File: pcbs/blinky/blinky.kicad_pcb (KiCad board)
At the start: 4 copper layers, 135 x 97 mm, 178 parts, among them J1 JACK IN, J3 CA1-9, J4 CB1-9, Q1 PMBT2222A,215, SW1 TACTILE, SW2 JS202011JCQN, U1 ATSAMD21E17, U2 MIC5225-3.3YM5, U3 TSOP36438TT, U4 IS31FL3731-SALS2

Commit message: Put all the passive values on silkscreen
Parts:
- C1: value 100uF 6.3V -> 100u
- C10, C11: value 10uF -> 10u
- C2, C7: value 1uF -> 1u
- C3, C4, C8, C9: value 0.1uF -> 0.1
- C5: value 1.0uF -> 1u
- C6: value 2.2uF -> 2.2
- R1: value 10kΩ -> 10k
- R2: value 330Ω -> 330
- R3: value 47Ω -> 47
- R4: value 470Ω -> 470
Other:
- board text added: "+"
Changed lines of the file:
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@@
   (general
     (thickness 1.6)
-    (drawings 20)
+    (drawings 21)
     (tracks 946)
     (zones 0)
@@
     (tags resistor)
     (attr smd)
-    (fp_text reference R10 (at -3.2 0 90) (layer F.SilkS)
+    (fp_text reference R10 (at -3.2 0 90) (layer F.Fab)
       (effects (font (size 1 1) (thickness 0.15)))
     )
-    (fp_text value 20K (at 0 1.43 90) (layer F.Fab)
+    (fp_text value 20K (at -2.969 0.023 90) (layer F.SilkS)
       (effects (font (size 1 1) (thickness 0.15)))
     )
@@
     (tags resistor)
     (attr smd)
-    (fp_text reference R9 (at 2.8 0 90) (layer F.SilkS)
+    (fp_text reference R9 (at 2.8 0 90) (layer F.Fab)
       (effects (font (size 1 1) (thickness 0.15)))
     )
-    (fp_text value 20K (at 0 1.43 90) (layer F.Fab)
+    (fp_text value 20K (at 2.969 -0.045 90) (layer F.SilkS)
       (effects (font (size 1 1) (thickness 0.15)))
     )
@@
     (tags resistor)
     (attr smd)
-    (fp_text reference R8 (at 2.8 0 90) (layer F.SilkS)
+    (fp_text reference R8 (at 2.8 0 90) (layer F.Fab)
       (effects (font (size 1 1) (thickness 0.15)))
     )
-    (fp_text value 20K (at 0 1.43 90) (layer F.Fab)
+    (fp_text value 20K (at 2.969 -0.194 90) (layer F.SilkS)
       (effects (font (size 1 1) (thickness 0.15)))
     )
@@
     (tags resistor)
     (attr smd)
-    (fp_text reference R7 (at -2.6 0 90) (layer F.SilkS)
+    (fp_text reference R7 (at -2.6 0 90) (layer F.Fab)
       (effects (font (size 1 1) (thickness 0.15)))
     )
-    (fp_text value 20K (at 0 1.43 90) (layer F.Fab)
+    (fp_text value 20K (at -3.111 0.067 90) (layer F.SilkS)
       (effects (font (size 1 1) (thickness 0.15)))
     )
@@
     (tags resistor)
     (attr smd)
-    (fp_text reference R6 (at 0 -1.43) (layer F.SilkS)
+    (fp_text reference R6 (at 0 -1.43) (layer F.Fab)
       (effects (font (size 1 1) (thickness 0.15)))
     )
-    (fp_text value 20K (at 0 1.43) (layer F.Fab)
+    (fp_text value 20K (at 0 -1.418) (layer F.SilkS)
       (effects (font (size 1 1) (thickness 0.15)))
     )
@@
     (tags resistor)
     (attr smd)
-    (fp_text reference R5 (at 0 -1.43) (layer F.SilkS)
+    (fp_text reference R5 (at 0 -1.43) (layer F.Fab)
       (effects (font (size 1 1) (thickness 0.15)))
     )
-    (fp_text value 20K (at 0 1.43) (layer F.Fab)
+    (fp_text value 20K (at 0.089 -1.481) (layer F.SilkS)
       (effects (font (size 1 1) (thickness 0.15)))
     )
@@
     (tags resistor)
     (attr smd)
-    (fp_text reference R4 (at -2.6 0 90) (layer F.SilkS)
+    (fp_text reference R4 (at -2.6 0 90) (layer F.Fab)
       (effects (font (size 1 1) (thickness 0.15)))
     )
-    (fp_text value 470Ω (at 0 1.43 90) (layer F.Fab)
+    (fp_text value 470 (at 2.96 0.15 90) (layer F.SilkS)
       (effects (font (size 1 1) (thickness 0.15)))
     )
@@
     (tags resistor)
     (attr smd)
-    (fp_text reference R3 (at 2.6 0 90) (layer F.SilkS)
+    (fp_text reference R3 (at 2.6 0 90) (layer F.Fab)
       (effects (font (size 1 1) (thickness 0.15)))
     )
-    (fp_text value 47Ω (at 0 1.43 90) (layer F.Fab)
+    (fp_text value 47 (at -2.706 -0.105 90) (layer F.SilkS)
       (effects (font (size 1 1) (thickness 0.15)))
     )
@@
     (tags resistor)
     (attr smd)
-    (fp_text reference R2 (at -2.8 0.2) (layer F.SilkS)
+    (fp_text reference R2 (at -2.8 0.2) (layer F.Fab)
       (effects (font (size 1 1) (thickness 0.15)))
     )
-    (fp_text value 330Ω (at 0 1.43) (layer F.Fab)
+    (fp_text value 330 (at -3.111 -0.097) (layer F.SilkS)
       (effects (font (size 1 1) (thickness 0.15)))
     )
@@
     (tags resistor)
     (attr smd)
-    (fp_text reference R1 (at -2.8 0) (layer F.SilkS)
+    (fp_text reference R1 (at -2.8 0) (layer F.Fab)
       (effects (font (size 1 1) (thickness 0.15)))
     )
-    (fp_text value 10kΩ (at 0 1.43) (layer F.Fab)
+    (fp_text value 10k (at -2.984 -0.192) (layer F.SilkS)
       (effects (font (size 1 1) (thickness 0.15)))
     )
@@
     (tags capacitor)
     (attr smd)
-    (fp_text reference C11 (at 3 0.2 90) (layer F.SilkS)
+    (fp_text reference C11 (at 3 0.2 90) (layer F.Fab)
       (effects (font (size 1 1) (thickness 0.15)))
     )
-    (fp_text value 10uF (at 0 1.43 90) (layer F.Fab)
+    (fp_text value 10u (at 2.984 -0.001 90) (layer F.SilkS)
       (effects (font (size 1 1) (thickness 0.15)))
     )
@@
     (tags capacitor)
     (attr smd)
-    (fp_text reference C10 (at 3 0 90) (layer F.SilkS)
+    (fp_text reference C10 (at 3 0 90) (layer F.Fab)
       (effects (font (size 1 1) (thickness 0.15)))
     )
-    (fp_text value 10uF (at 0 1.43 90) (layer F.Fab)
+    (fp_text value 10u (at 2.984 -0.023 90) (layer F.SilkS)
       (effects (font (size 1 1) (thickness 0.15)))
     )
@@
     (tags capacitor)
     (attr smd)
-    (fp_text reference C9 (at 2.6 0 90) (layer F.SilkS)
+    (fp_text reference C9 (at 2.6 0 90) (layer F.Fab)
       (effects (font (size 1 1) (thickness 0.15)))
     )
-    (fp_text value 0.1uF (at 0 1.43 90) (layer F.Fab)
+    (fp_text value 0.1 (at 2.857 -0.045 90) (layer F.SilkS)
       (effects (font (size 1 1) (thickness 0.15)))
     )
@@
     (tags capacitor)
     (attr smd)
-    (fp_text reference C8 (at -2.8 0 90) (layer F.SilkS)
+    (fp_text reference C8 (at -2.8 0 90) (layer F.Fab)
       (effects (font (size 1 1) (thickness 0.15)))
     )
-    (fp_text value 0.1uF (at 0 1.43 90) (layer F.Fab)
+    (fp_text value 0.1 (at -2.588 0.001 90) (layer F.SilkS)
       (effects (font (size 1 1) (thickness 0.15)))
     )
@@
     (tags capacitor)
     (attr smd)
-    (fp_text reference C7 (at -2.6 0.2 90) (layer F.SilkS)
+    (fp_text reference C7 (at -2.6 0.2 90) (layer F.Fab)
       (effects (font (size 1 1) (thickness 0.15)))
     )
-    (fp_text value 1uF (at 0 1.43 90) (layer F.Fab)
+    (fp_text value 1u (at 2.96 -0.063 90) (layer F.SilkS)
       (effects (font (size 1 1) (thickness 0.15)))
     )
@@
     (tags capacitor)
     (attr smd)
-    (fp_text reference C6 (at -3 0 90) (layer F.SilkS)
+    (fp_text reference C6 (at -3 0 90) (layer F.Fab)
       (effects (font (size 1 1) (thickness 0.15)))
     )
-    (fp_text value 2.2uF (at 0 1.43 90) (layer F.Fab)
+    (fp_text value 2.2 (at -3.302 -0.127 180) (layer F.SilkS)
       (effects (font (size 1 1) (thickness 0.15)))
     )
@@
     (tags capacitor)
     (attr smd)
-    (fp_text reference C5 (at -3.048 0.127 90) (layer F.SilkS)
+    (fp_text reference C5 (at -3.048 0.127 90) (layer F.Fab)
       (effects (font (size 1 1) (thickness 0.15)))
     )
-    (fp_text value 1.0uF (at 0 1.43 90) (layer F.Fab)
+    (fp_text value 1u (at -3.302 0 180) (layer F.SilkS)
       (effects (font (size 1 1) (thickness 0.15)))
     )
@@
     (tags capacitor)
     (attr smd)
-    (fp_text reference C4 (at 2.8 0) (layer F.SilkS)
+    (fp_text reference C4 (at 2.8 0) (layer F.Fab)
       (effects (font (size 1 1) (thickness 0.15)))
     )
-    (fp_text value 0.1uF (at 0 1.43) (layer F.Fab)
+    (fp_text value 0.1 (at 2.857 -0.094) (layer F.SilkS)
       (effects (font (size 1 1) (thickness 0.15)))
     )
@@
     (tags capacitor)
     (attr smd)
-    (fp_text reference C3 (at 2.413 0 180) (layer F.SilkS)
+    (fp_text reference C3 (at 2.413 0 180) (layer F.Fab)
       (effects (font (size 1 1) (thickness 0.15)))
     )
-    (fp_text value 0.1uF (at 0 1.43 90) (layer F.Fab)
+    (fp_text value 0.1 (at 2.159 0 180) (layer F.SilkS)
       (effects (font (size 1 1) (thickness 0.15)))
     )
@@
     (tags capacitor)
     (attr smd)
-    (fp_text reference C2 (at 2.413 0.127 180) (layer F.SilkS)
+    (fp_text reference C2 (at 2.413 0.127 180) (layer F.Fab)
       (effects (font (size 1 1) (thickness 0.15)))
     )
-    (fp_text value 1uF (at 0 1.43 90) (layer F.Fab)
+    (fp_text value 1u (at 2.413 0 180) (layer F.SilkS)
       (effects (font (size 1 1) (thickness 0.15)))
     )
@@
     (tags capacitor)
     (attr smd)
-    (fp_text reference C1 (at -3.937 0.127 270) (layer F.SilkS)
+    (fp_text reference C1 (at -3.937 0.127 270) (layer F.Fab)
       (effects (font (size 1 1) (thickness 0.15)))
     )
-    (fp_text value "100uF 6.3V" (at 0 1.85 90) (layer F.Fab)
+    (fp_text value 100u (at -4.953 0.127 90) (layer F.SilkS)
       (effects (font (size 1 1) (thickness 0.15)))
     )
@@
     )
   )
+  (gr_text + (at 99.993 141.575) (layer F.SilkS)
+    (effects (font (size 1 1) (thickness 0.15)))
+  )
   (gr_text OFF (at 56.94 140.559) (layer F.SilkS)
     (effects (font (size 1 1) (thickness 0.15)))
@@
   (segment (start 76.278 98.304) (end 94.272 98.304) (width 0.2) (layer In1.Cu) (net 14))
   (segment (start 71.926 102.656) (end 76.278 98.304) (width 0.2) (layer In1.Cu) (net 14))
-  (segment (start 99.247 115.304) (end 99.272 115.279) (width 0.2) (layer F.Cu) (net 14))
-  (segment (start 95.072 115.304) (end 99.247 115.304) (width 0.2) (layer F.Cu) (net 14))
-  (segment (start 95.072 115.304) (end 94.672 113.704) (width 0.2) (layer In1.Cu) (net 14))
-  (segment (start 94.472 98.504) (end 94.272 98.304) (width 0.2) (layer In1.Cu) (net 14))
   (segment (start 94.672 98.704) (end 94.472 98.504) (width 0.2) (layer In1.Cu) (net 14))
   (segment (start 94.672 113.704) (end 94.672 98.704) (width 0.2) (layer In1.Cu) (net 14))
-  (via (at 95.072 115.304) (size 0.6) (drill 0.3) (layers F.Cu B.Cu) (net 14))
+  (segment (start 94.472 98.504) (end 94.272 98.304) (width 0.2) (layer In1.Cu) (net 14))
+  (via (at 94.659 115.286) (size 0.6) (drill 0.3) (layers F.Cu B.Cu) (net 14))
+  (segment (start 94.659 115.286) (end 94.672 113.704) (width 0.2) (layer In1.Cu) (net 14))
+  (segment (start 99.247 115.304) (end 99.272 115.279) (width 0.2) (layer F.Cu) (net 14))
+  (segment (start 94.659 115.286) (end 99.247 115.304) (width 0.2) (layer F.Cu) (net 14))
   (via (at 72.823 108.684) (size 0.6) (drill 0.3) (layers F.Cu B.Cu) (net 15))
   (via (at 72.823 111.354) (size 0.6) (drill 0.3) (layers F.Cu B.Cu) (net 15))

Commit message: route sda/scl across the middle
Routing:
- net /SCL: track 124.1 -> 75.7 mm
- net /SDA: track 120.1 -> 73.1 mm, vias 0 -> 2
- net /CB1: track 102.2 -> 104.7 mm, vias 8 -> 7

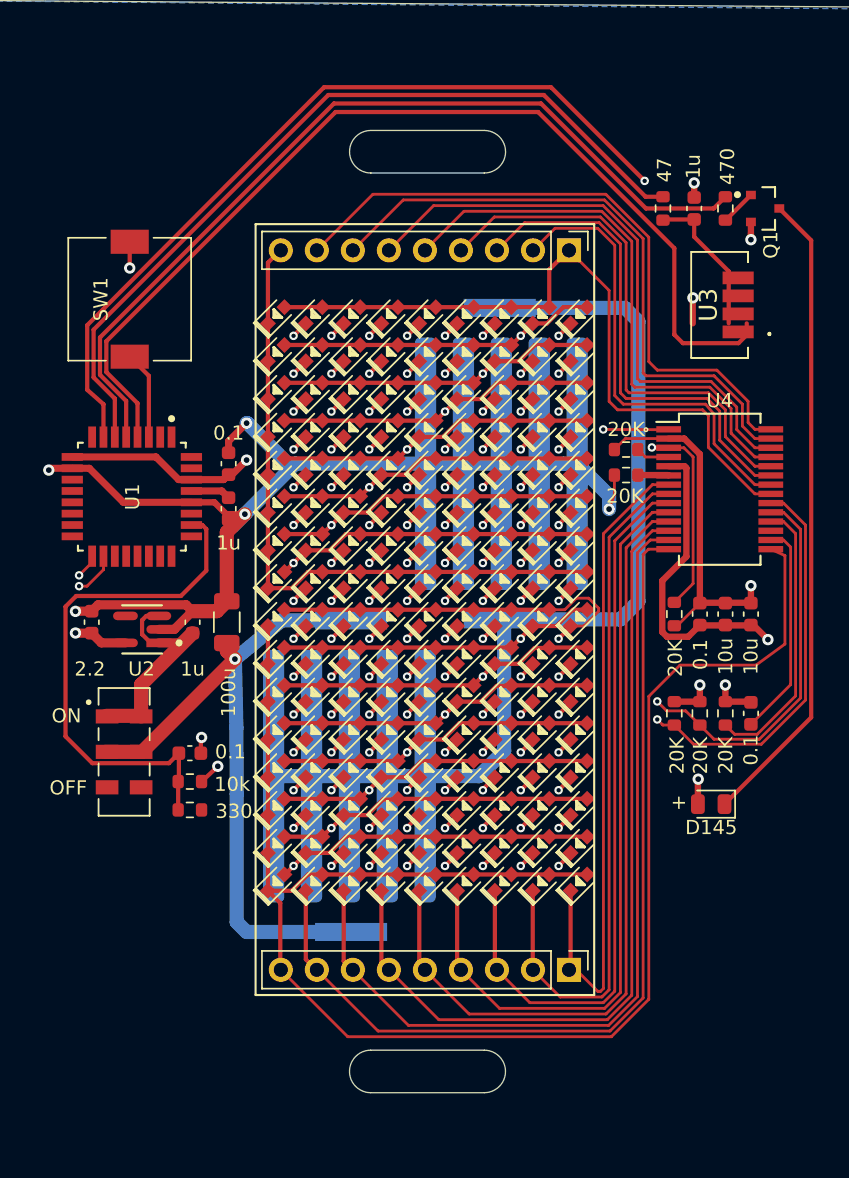
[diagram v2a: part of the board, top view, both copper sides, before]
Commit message: tidied up a bit more routing to make board smaller
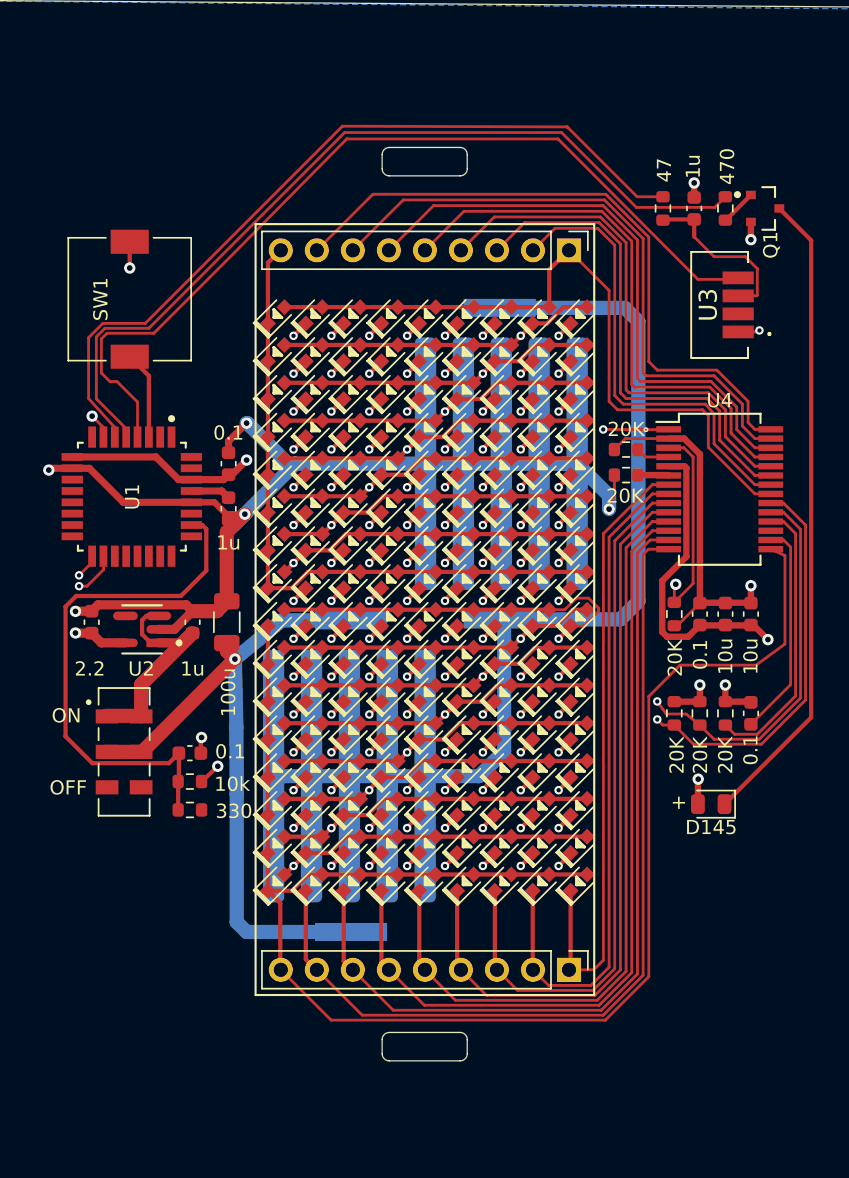
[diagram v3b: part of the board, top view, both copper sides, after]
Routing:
- net /A6: track 90.5 -> 68.1 mm
- net /A1: track 70.9 -> 62.1 mm
- net /CB1: track 104.7 -> 102.8 mm
- net /CB9: track 116.3 -> 114.4 mm
- net /CB8: track 119.0 -> 117.1 mm
- net /CB7: track 116.2 -> 114.4 mm
- net /CB6: track 113.5 -> 111.7 mm
- net /CB5: track 110.9 -> 109.2 mm
- net /A3: track 58.2 -> 56.4 mm
- net /CB4: track 108.3 -> 106.6 mm
- net /CB3: track 105.7 -> 104.0 mm
- net /CB2: track 103.0 -> 101.4 mm
- net Net-(C7-Pad1): track 10.6 -> 12.1 mm
- net /A2: track 62.1 -> 60.8 mm
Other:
- outline, holes or cut-outs redrawn

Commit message: lots of beautiful decorations
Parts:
- moved Q1 42.3 mm to (100.7, 141.7)
- moved J1 23.7 mm to (65.7, 155.3), turned to 323 degrees
- moved D145 3.81 mm to (106.1, 141.5), turned to 0 degrees
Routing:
- net (no net): track 0.00 -> 270.2 mm
- net Net-(Q1-Pad1): track 2.54 -> 49.2 mm
- net /A7: track 0.00 -> 46.1 mm
- net Net-(D145-Pad1): track 45.5 -> 3.55 mm
- net /SWDIO: track 0.00 -> 41.5 mm, vias 0 -> 1
- net /SWCLK: track 0.00 -> 39.1 mm, vias 0 -> 1
- net /~RESET: track 0.00 -> 15.2 mm, vias 0 -> 1
- net VBUS: track 49.2 -> 55.0 mm, vias 1 -> 2
- net +3V3: track 48.2 -> 50.3 mm, vias 6 -> 7
- net GND: track 110.7 -> 111.7 mm, vias 12 -> 13
- added copper zone on F.Cu, net (none)
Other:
- board size 135 x 97 mm -> 91 x 93 mm

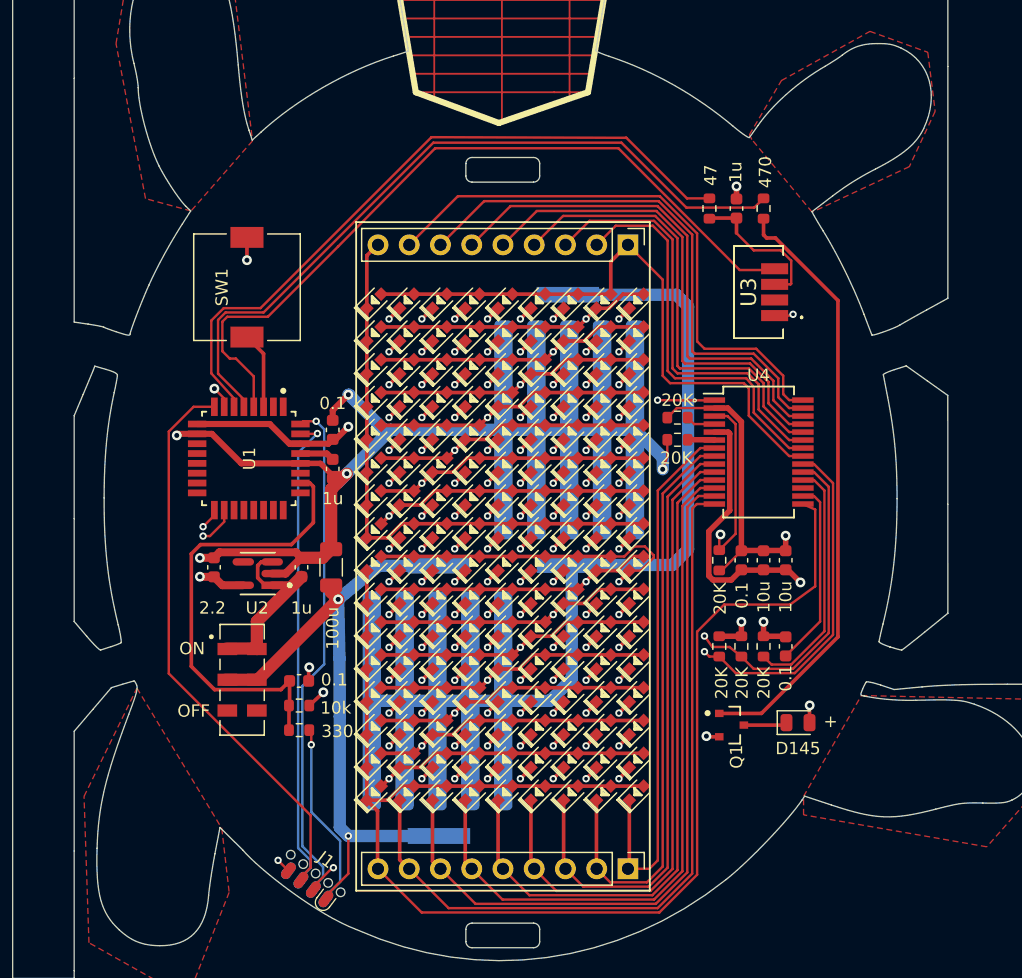
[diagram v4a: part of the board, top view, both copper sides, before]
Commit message: mousebite improvements
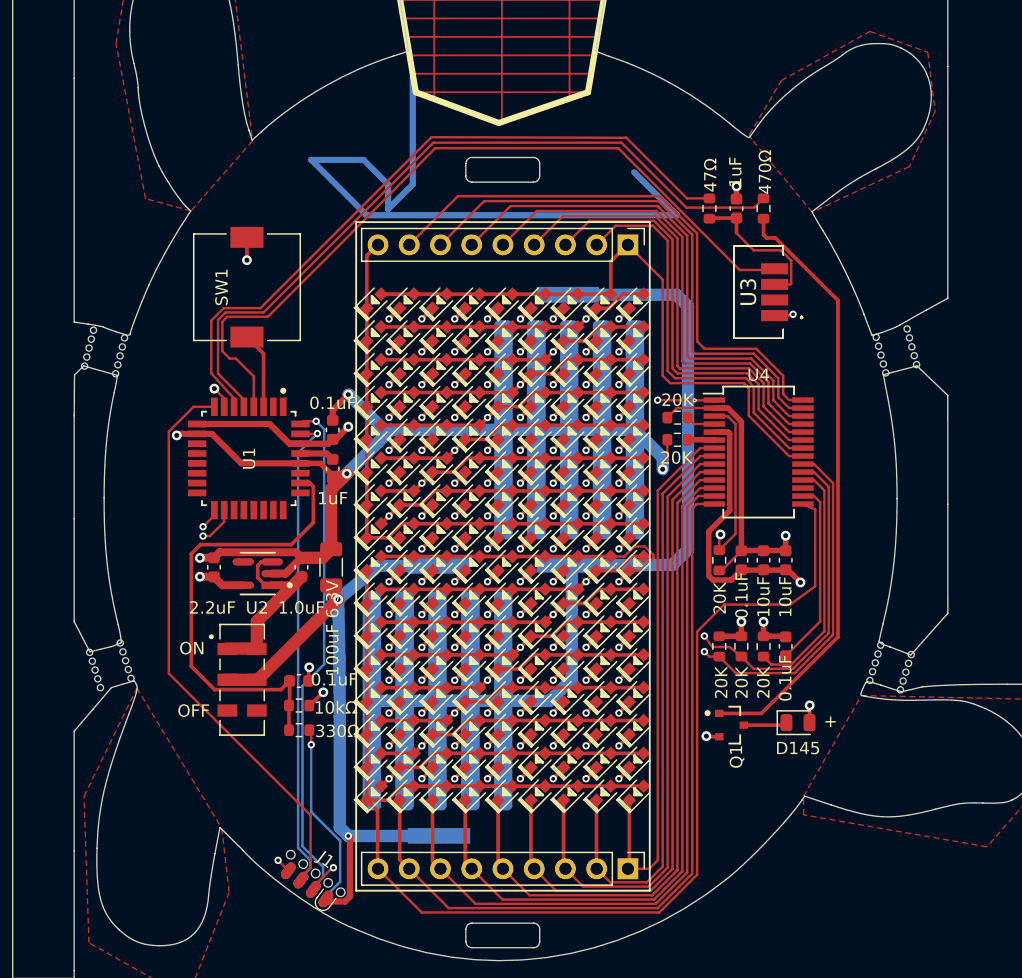
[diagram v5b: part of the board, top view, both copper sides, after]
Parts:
- added H1: Mouse Bite, Joels KiCad Footprint Library:Mouse_Bite_For_Clipper, F.Cu at (51.5, 109.5)
- added H2: Mouse Bite, Joels KiCad Footprint Library:Mouse_Bite_For_Clipper, F.Cu at (50.8, 134.3)
- added H3: Mouse Bite, Joels KiCad Footprint Library:Mouse_Bite_For_Clipper, F.Cu at (114.8, 108.8)
- added H4: Mouse Bite, Joels KiCad Footprint Library:Mouse_Bite_For_Clipper, F.Cu at (115.5, 135.2)
- C1: value 100u -> 100uF 6.3V
- C10, C11: value 10u -> 10uF
- C2, C7: value 1u -> 1uF
- C3, C4, C8, C9: value 0.1 -> 0.1uF
- C5: value 1u -> 1.0uF
- C6: value 2.2 -> 2.2uF
- R1: value 10k -> 10kΩ
- R2: value 330 -> 330Ω
- R3: value 47 -> 47Ω
- R4: value 470 -> 470Ω
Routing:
- net +3V3: track 50.3 -> 107.5 mm
- net VBUS: track 55.0 -> 56.3 mm
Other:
- outline, holes or cut-outs redrawn
